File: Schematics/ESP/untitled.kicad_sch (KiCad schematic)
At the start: 9 parts, among them J1 Conn_01x04_Male, J10 Conn_01x03_Socket, J11 Conn_01x02_Pin, J12 Conn_01x02_Pin, J2 Conn_01x04_Male, J9 Conn_01x03_Socket, U1 NUCLEO64-F411RE

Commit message: some pcb changes
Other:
- moved on the sheet: J1
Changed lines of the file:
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@@
   (no_connect (at 156.21 135.89))
   (no_connect (at 212.09 82.55))
-  (wire (pts (xy 132.08 125.73) (xy 132.08 128.27))
+  (wire (pts (xy 125.73 125.73) (xy 125.73 128.27))
     (stroke (width 0) (type default))
   )
@@
     (stroke (width 0) (type default))
   )
-  (wire (pts (xy 142.24 115.57) (xy 156.21 115.57))
-    (stroke (width 0) (type default))
-  )
   (wire (pts (xy 147.32 100.33) (xy 147.32 96.52))
     (stroke (width 0) (type default))
@@
     (stroke (width 0) (type default))
   )
-  (wire (pts (xy 142.24 115.57) (xy 142.24 123.19))
+  (wire (pts (xy 135.89 115.57) (xy 135.89 123.19))
     (stroke (width 0) (type default))
   )
@@
     (stroke (width 0) (type default))
   )
-  (wire (pts (xy 139.7 113.03) (xy 156.21 113.03))
-    (stroke (width 0) (type default))
-  )
   (wire (pts (xy 176.53 147.32) (xy 176.53 146.05))
     (stroke (width 0) (type default))
@@
     (stroke (width 0) (type default))
   )
-  (wire (pts (xy 130.81 125.73) (xy 132.08 125.73))
+  (wire (pts (xy 133.35 113.03) (xy 156.21 113.03))
+    (stroke (width 0) (type default))
+  )
+  (wire (pts (xy 124.46 125.73) (xy 125.73 125.73))
     (stroke (width 0) (type default))
   )
@@
     (stroke (width 0) (type default))
   )
-  (wire (pts (xy 139.7 120.65) (xy 130.81 120.65))
+  (wire (pts (xy 133.35 120.65) (xy 124.46 120.65))
     (stroke (width 0) (type default))
   )
@@
     (stroke (width 0) (type default))
   )
-  (wire (pts (xy 132.08 118.11) (xy 132.08 114.3))
+  (wire (pts (xy 125.73 118.11) (xy 125.73 114.3))
     (stroke (width 0) (type default))
   )
@@
     (stroke (width 0) (type default))
   )
-  (wire (pts (xy 130.81 118.11) (xy 132.08 118.11))
+  (wire (pts (xy 124.46 118.11) (xy 125.73 118.11))
     (stroke (width 0) (type default))
   )
@@
     (stroke (width 0) (type default))
   )
-  (wire (pts (xy 142.24 123.19) (xy 130.81 123.19))
+  (wire (pts (xy 135.89 123.19) (xy 124.46 123.19))
     (stroke (width 0) (type default))
   )
@@
     (stroke (width 0) (type default))
   )
+  (wire (pts (xy 135.89 115.57) (xy 156.21 115.57))
+    (stroke (width 0) (type default))
+  )
   (wire (pts (xy 212.09 123.19) (xy 232.41 123.19))
     (stroke (width 0) (type default))
@@
     (stroke (width 0) (type default))
   )
-  (wire (pts (xy 139.7 113.03) (xy 139.7 120.65))
+  (wire (pts (xy 133.35 113.03) (xy 133.35 120.65))
     (stroke (width 0) (type default))
   )
@@
   (text "I2C2_SDA" (at 213.36 123.19 0)
     (effects (font (size 1.27 1.27)) (justify left bottom))
+  )
+  (global_label "+5V" (shape input) (at 125.73 114.3 90) (fields_autoplaced)
+    (effects (font (size 1.27 1.27)) (justify left))
+    (property "Intersheetrefs" "${INTERSHEET_REFS}" (at 125.73 107.5237 90)
+      (effects (font (size 1.27 1.27)) (justify left) hide)
+    )
   )
   (global_label "Bumper Button 1" (shape output) (at 68.58 63.5 0) (fields_autoplaced)
@@
     )
   )
+  (global_label "+5V" (shape input) (at 251.46 124.46 90) (fields_autoplaced)
+    (effects (font (size 1.27 1.27)) (justify left))
+    (property "Intersheetrefs" "${INTERSHEET_REFS}" (at 251.46 117.6837 90)
+      (effects (font (size 1.27 1.27)) (justify left) hide)
+    )
+  )
   (global_label "+5V" (shape input) (at 54.61 109.22 90) (fields_autoplaced)
     (effects (font (size 1.27 1.27)) (justify left))
@@
     )
   )
+  (global_label "+5V" (shape input) (at 236.22 118.11 90) (fields_autoplaced)
+    (effects (font (size 1.27 1.27)) (justify left))
+    (property "Intersheetrefs" "${INTERSHEET_REFS}" (at 236.22 111.3337 90)
+      (effects (font (size 1.27 1.27)) (justify left) hide)
+    )
+  )
   (global_label "Motion Sensor A" (shape input) (at 147.32 102.87 180) (fields_autoplaced)
     (effects (font (size 1.27 1.27)) (justify right))
@@
     )
   )
-  (symbol (lib_id "power:+5V") (at 132.08 114.3 0) (unit 1)
-    (in_bom yes) (on_board yes) (dnp no)
-    (property "Reference" "#PWR?" (at 132.08 118.11 0)
-      (effects (font (size 1.27 1.27)) hide)
-    )
-    (property "Value" "+5V" (at 129.54 111.76 0)
-      (effects (font (size 1.27 1.27)))
-    )
-    (property "Footprint" "" (at 132.08 114.3 0)
-      (effects (font (size 1.27 1.27)) hide)
-    )
-    (property "Datasheet" "" (at 132.08 114.3 0)
-      (effects (font (size 1.27 1.27)) hide)
-    )
-    (pin "1")
-    (instances
-      (project "ESP"
-        (path "/b616d203-cf5c-462f-b907-860a8573592a"
-          (reference "#PWR?") (unit 1)
-        )
-        (path "/b616d203-cf5c-462f-b907-860a8573592a/d73e0648-2dfb-47f8-9e43-38f378a4f4ca"
-          (reference "#PWR01") (unit 1)
-        )
-      )
-    )
-  )
   (symbol (lib_id "Device:R") (at 245.11 128.27 0) (unit 1)
     (in_bom yes) (on_board yes) (dnp no) (fields_autoplaced)
@@
     )
   )
-  (symbol (lib_id "Connector:Conn_01x04_Male") (at 125.73 120.65 0) (unit 1)
+  (symbol (lib_id "Connector:Conn_01x04_Male") (at 119.38 120.65 0) (unit 1)
     (in_bom yes) (on_board yes) (dnp no)
-    (property "Reference" "J1" (at 124.46 114.3 0)
+    (property "Reference" "J1" (at 118.11 114.3 0)
       (effects (font (size 1.27 1.27)))
     )
-    (property "Value" "Conn_01x04_Male" (at 119.38 129.54 0)
+    (property "Value" "Conn_01x04_Male" (at 113.03 129.54 0)
       (effects (font (size 1.27 1.27)))
     )
-    (property "Footprint" "Connector_PinSocket_1.00mm:PinSocket_1x04_P1.00mm_Vertical" (at 125.73 120.65 0)
-      (effects (font (size 1.27 1.27)) hide)
-    )
-    (property "Datasheet" "~" (at 125.73 120.65 0)
-      (effects (font (size 1.27 1.27)) hide)
-    )
-    (property "digikey link" "https://www.digikey.fi/fi/products/detail/kyocera-avx/009276004021106/2346141" (at 125.73 120.65 0)
-      (effects (font (size 1.27 1.27)) hide)
-    )
-    (property "Price" "1,29" (at 125.73 120.65 0)
+    (property "Footprint" "Connector_PinSocket_1.00mm:PinSocket_1x04_P1.00mm_Vertical" (at 119.38 120.65 0)
+      (effects (font (size 1.27 1.27)) hide)
+    )
+    (property "Datasheet" "~" (at 119.38 120.65 0)
+      (effects (font (size 1.27 1.27)) hide)
+    )
+    (property "digikey link" "https://www.digikey.fi/fi/products/detail/kyocera-avx/009276004021106/2346141" (at 119.38 120.65 0)
+      (effects (font (size 1.27 1.27)) hide)
+    )
+    (property "Price" "1,29" (at 119.38 120.65 0)
       (effects (font (size 1.27 1.27)) hide)
     )
@@
     )
   )
-  (symbol (lib_id "power:GND") (at 132.08 128.27 0) (unit 1)
+  (symbol (lib_id "power:GND") (at 125.73 128.27 0) (unit 1)
     (in_bom yes) (on_board yes) (dnp no) (fields_autoplaced)
-    (property "Reference" "#PWR?" (at 132.08 134.62 0)
-      (effects (font (size 1.27 1.27)) hide)
-    )
-    (property "Value" "GND" (at 132.08 133.35 0)
+    (property "Reference" "#PWR?" (at 125.73 134.62 0)
+      (effects (font (size 1.27 1.27)) hide)
+    )
+    (property "Value" "GND" (at 125.73 133.35 0)
       (effects (font (size 1.27 1.27)))
     )
-    (property "Footprint" "" (at 132.08 128.27 0)
-      (effects (font (size 1.27 1.27)) hide)
-    )
-    (property "Datasheet" "" (at 132.08 128.27 0)
+    (property "Footprint" "" (at 125.73 128.27 0)
+      (effects (font (size 1.27 1.27)) hide)
+    )
+    (property "Datasheet" "" (at 125.73 128.27 0)
       (effects (font (size 1.27 1.27)) hide)
     )
@@
         )
       )
-    )
-  )
-  (symbol (lib_id "power:+5V") (at 236.22 118.11 0) (unit 1)
-    (in_bom yes) (on_board yes) (dnp no) (fields_autoplaced)
-    (property "Reference" "#PWR?" (at 236.22 121.92 0)
-      (effects (font (size 1.27 1.27)) hide)
-    )
-    (property "Value" "+5V" (at 236.22 113.03 0)
-      (effects (font (size 1.27 1.27)))
-    )
-    (property "Footprint" "" (at 236.22 118.11 0)
-      (effects (font (size 1.27 1.27)) hide)
-    )
-    (property "Datasheet" "" (at 236.22 118.11 0)
-      (effects (font (size 1.27 1.27)) hide)
-    )
-    (pin "1")
-    (instances
-      (project "ESP"
-        (path "/b616d203-cf5c-462f-b907-860a8573592a"
-          (reference "#PWR?") (unit 1)
-        )
-        (path "/b616d203-cf5c-462f-b907-860a8573592a/d73e0648-2dfb-47f8-9e43-38f378a4f4ca"
-          (reference "#PWR05") (unit 1)
-        )
-      )
-    )
-  )
-  (symbol (lib_id "power:+5V") (at 251.46 124.46 0) (unit 1)
-    (in_bom yes) (on_board yes) (dnp no) (fields_autoplaced)
-    (property "Reference" "#PWR?" (at 251.46 128.27 0)
-      (effects (font (size 1.27 1.27)) hide)
-    )
-    (property "Value" "+5V" (at 251.46 119.38 0)
-      (effects (font (size 1.27 1.27)))
-    )
-    (property "Footprint" "" (at 251.46 124.46 0)
-      (effects (font (size 1.27 1.27)) hide)
-    )
-    (property "Datasheet" "" (at 251.46 124.46 0)
-      (effects (font (size 1.27 1.27)) hide)
-    )
-    (pin "1")
-    (instances
-      (project "ESP"
-        (path "/b616d203-cf5c-462f-b907-860a8573592a"
-          (reference "#PWR?") (unit 1)
-        )
-        (path "/b616d203-cf5c-462f-b907-860a8573592a/d73e0648-2dfb-47f8-9e43-38f378a4f4ca"
-          (reference "#PWR026") (unit 1)
-        )
-      )

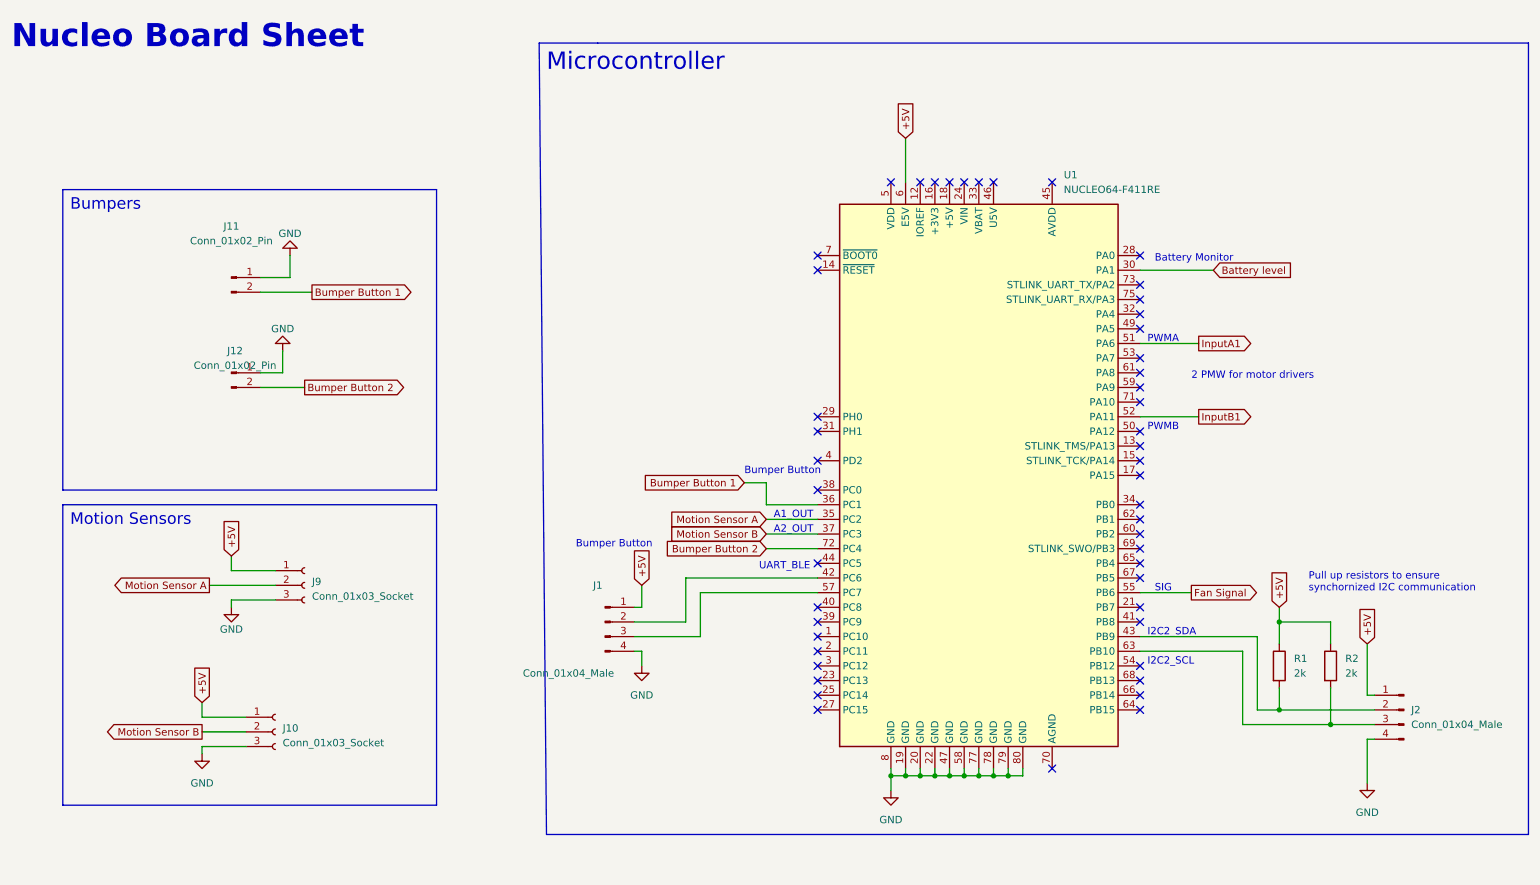
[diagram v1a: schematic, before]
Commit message: Changed schematics and PCB for shield
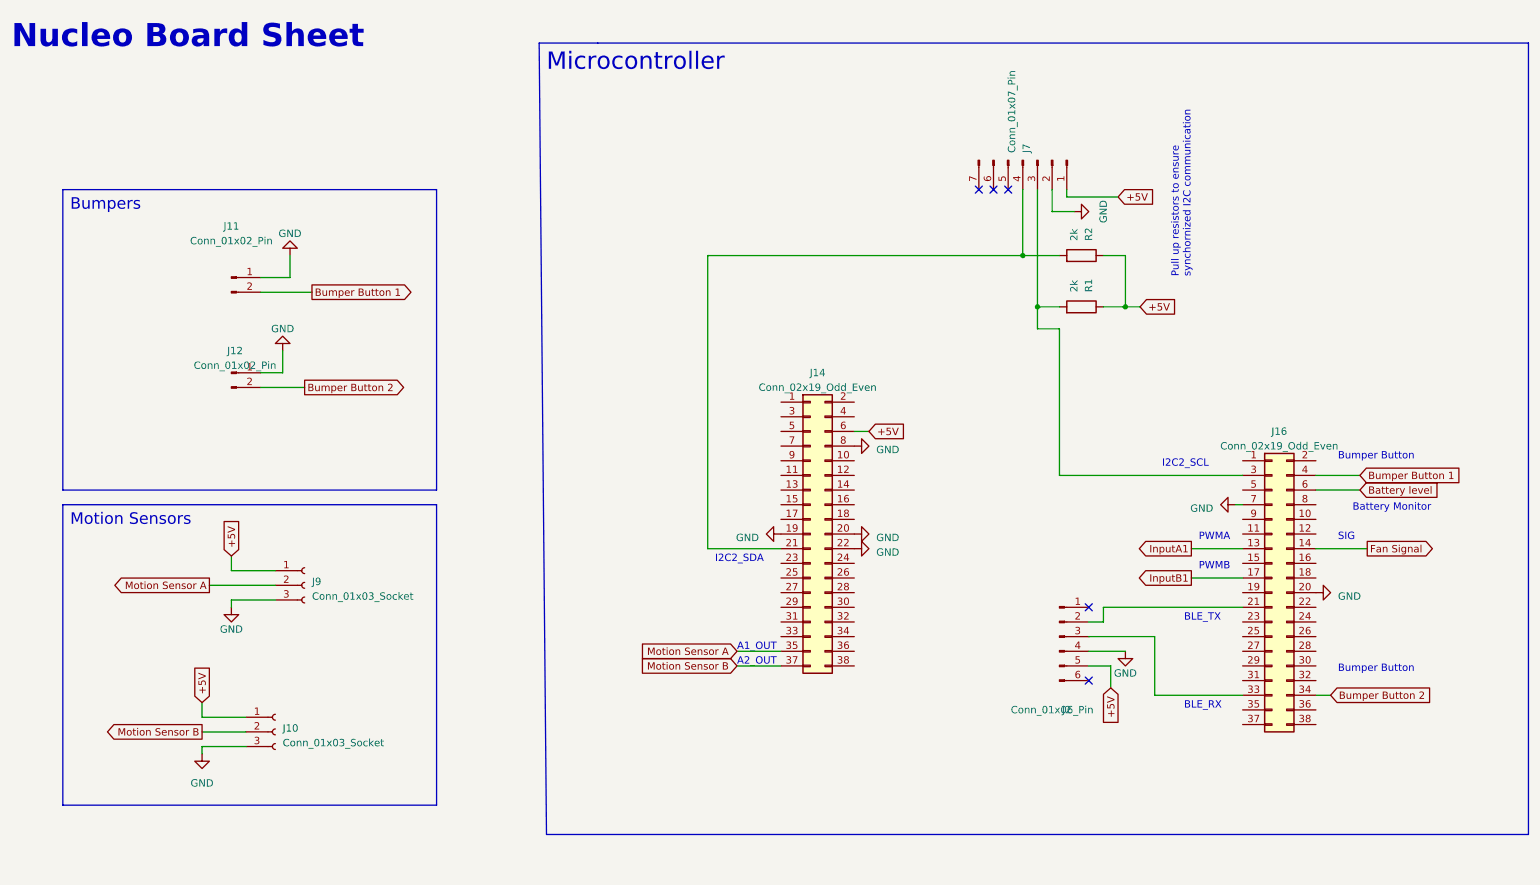
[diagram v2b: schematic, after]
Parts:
- removed J1, J2: Conn_01x04_Male, Connector_PinSocket_1.00mm:PinSocket_1x04_P1.00mm_Vertical, symbol Connector:Conn_01x04_Male
- removed U1: NUCLEO64-F411RE, Module:ST_Morpho_Connector_144_STLink, symbol MCU_Module:NUCLEO64-F411RE
- added J14, J16: Conn_02x19_Odd_Even, Connector_PinSocket_2.54mm:PinSocket_2x19_P2.54mm_Vertical, symbol Connector_Generic:Conn_02x19_Odd_Even
- added J2: Conn_01x06_Pin, Connector_PinSocket_2.54mm:PinSocket_1x06_P2.54mm_Vertical, symbol Connector:Conn_01x06_Pin
- added J7: Conn_01x07_Pin, Connector_PinSocket_2.54mm:PinSocket_1x07_P2.54mm_Vertical, symbol Connector:Conn_01x07_Pin
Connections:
- net +5V: now also J14.6 (Pin_6), J2.5 (Pin_5), J7.1 (Pin_1)
- net Battery level: now also J16.6 (Pin_6)
- net Bumper Button 1: now also J16.4 (Pin_4)
- net Bumper Button 2: now also J16.34 (Pin_34)
- net Fan Signal: now also J16.14 (Pin_14)
- net GND: now also J14.19 (Pin_19), J14.20 (Pin_20), J14.22 (Pin_22), J14.8 (Pin_8), J16.20 (Pin_20), J16.7 (Pin_7), J2.4 (Pin_4), J7.2 (Pin_2)
- net InputA1: now also J16.13 (Pin_13)
- net InputB1: now also J16.17 (Pin_17)
- net Motion Sensor A: now also J14.35 (Pin_35)
- net Motion Sensor B: now also J14.37 (Pin_37)
- net at R2.2: now also J14.21 (Pin_21), J7.4 (Pin_4)
- net at R1.2: now also J16.3 (Pin_3), J7.3 (Pin_3)
- new net: J16.21 (Pin_21), J2.2 (Pin_2)
- new net: J16.33 (Pin_33), J2.3 (Pin_3)
- no-connect marks 49 -> 5
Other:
- note added: "BLE_RX"
- note added: "BLE_TX"
- note removed: "2 PMW for motor drivers"
- note removed: "UART_BLE"
- moved on the sheet: R1, R2

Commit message: Can Pull
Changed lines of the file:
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@@
       (effects (font (size 1.27 1.27)))
     )
-    (property "Value" "Conn_01x06_Pin" (at 196.85 135.89 0)
+    (property "Value" "Conn_01x06_Pin" (at 198.12 142.24 0)
       (effects (font (size 1.27 1.27)))
     )

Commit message: Can Pull
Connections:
- net GND: now also J16.9 (Pin_9); no longer J16.7 (Pin_7)
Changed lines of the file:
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@@
-    (stroke (width 0) (type default))
-  )
-  (wire (pts (xy 228.6 100.33) (xy 229.87 100.33))
     (stroke (width 0) (type default))
   )
@@
   )
   (text "Pull up resistors to ensure \nsynchornized I2C communication"
-    (at 220.98 60.96 90)
-    (effects (font (size 1.27 1.27)) (justify left bottom))
+    (at 190.5 66.04 0)
+    (effects (font (size 1.27 1.27)) (justify right bottom))
   )
   (text "Battery Monitor" (at 248.92 101.6 0)
@@
     )
   )
-  (symbol (lib_id "power:GND") (at 228.6 100.33 270) (unit 1)
-    (in_bom yes) (on_board yes) (dnp no) (fields_autoplaced)
-    (property "Reference" "#PWR?" (at 222.25 100.33 0)
-      (effects (font (size 1.27 1.27)) hide)
-    )
-    (property "Value" "GND" (at 224.79 100.965 90)
+  (symbol (lib_id "power:GND") (at 229.87 102.87 270) (unit 1)
+    (in_bom yes) (on_board yes) (dnp no) (fields_autoplaced)
+    (property "Reference" "#PWR?" (at 223.52 102.87 0)
+      (effects (font (size 1.27 1.27)) hide)
+    )
+    (property "Value" "GND" (at 226.06 103.505 90)
       (effects (font (size 1.27 1.27)) (justify right))
     )
-    (property "Footprint" "" (at 228.6 100.33 0)
-      (effects (font (size 1.27 1.27)) hide)
-    )
-    (property "Datasheet" "" (at 228.6 100.33 0)
-      (effects (font (size 1.27 1.27)) hide)
-    )
+    (property "Footprint" "" (at 229.87 102.87 0)
+      (effects (font (size 1.27 1.27)) hide)
+    )
+    (property "Datasheet" "" (at 229.87 102.87 0)
+      (effects (font (size 1.27 1.27)) hide)
+    )
